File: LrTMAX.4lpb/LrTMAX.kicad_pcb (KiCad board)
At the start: 4 copper layers, 100 x 100 mm, 126 parts, among them J1 USB_C_Receptacle_USB2.0, J2 Conn_02x05_Odd_Even, Q1 2N7002, SW1 Tact_SW_8mm, SW10 EC11_SMD, SW11 EC11_SMD, SW12 EC11_SMD, SW13 EC11_SMD, SW14 EC11_SMD, SW15 EC11_SMD, SW16 EC11_SMD, SW17 EC11_SMD, SW2 Tact_SW_8mm, SW20 SW_SPST, SW3 Tact_SW_8mm, SW4 Tact_SW_8mm, SW5 Tact_SW_8mm, SW6 Tact_SW_8mm, SW7 Tact_SW_8mm, SW8 Tact_SW_8mm, U1 STM32F072C8Tx, U3 SSD1306_OLED_0.91, U4 SPX3819M5-L3-3TR

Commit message: Refine pattern.
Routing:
- net /M3: track 197.1 -> 196.4 mm
- net GND: track 46.4 -> 45.8 mm
- net /USB_DM: track 29.5 -> 28.9 mm
- net Net-(R45-Pad1): track 14.8 -> 14.2 mm
- net /ENC1B: track 80.6 -> 80.1 mm
- net /ENC4A: track 41.5 -> 41.0 mm

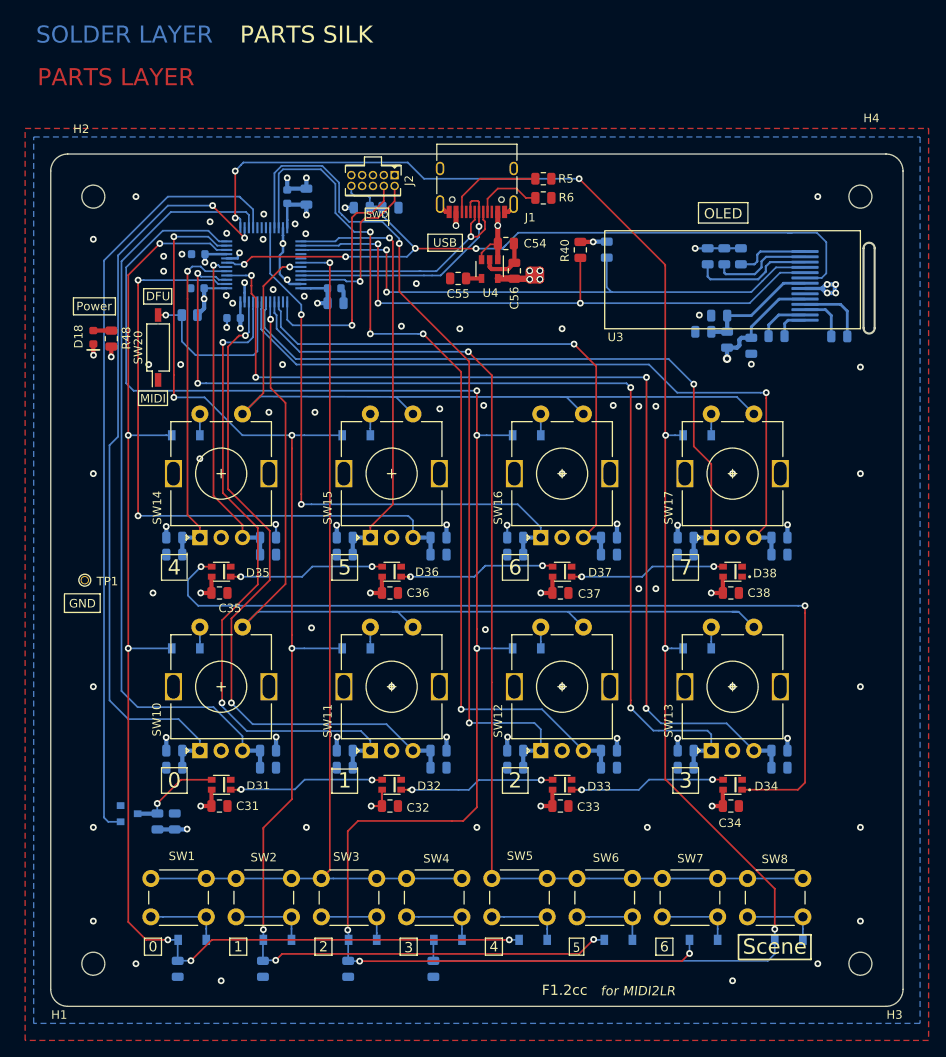
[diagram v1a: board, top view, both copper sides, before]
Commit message: Flex wire hall refined
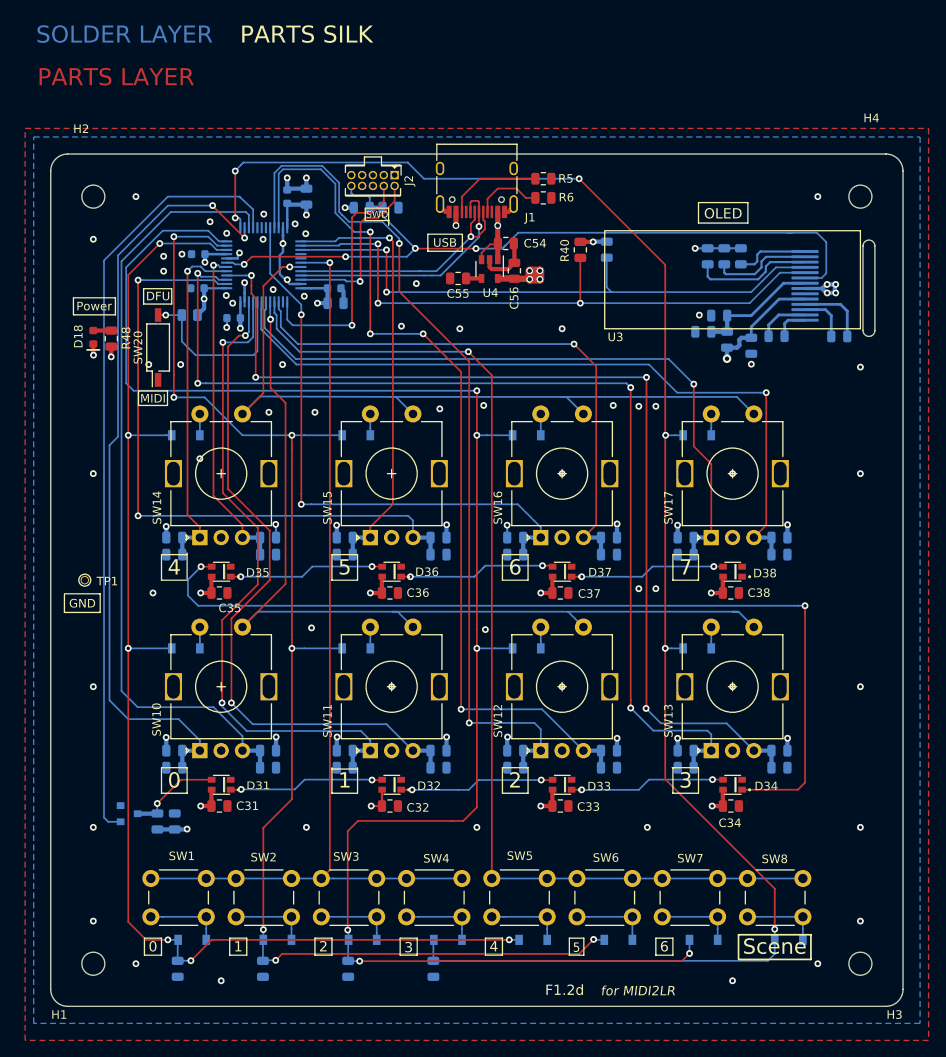
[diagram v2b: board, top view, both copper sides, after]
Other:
- outline, holes or cut-outs redrawn
- rule pad_to_mask_clearance: 0.051 -> 0
- board text added: "F1.2d"
- board text removed: "F1.2cc"
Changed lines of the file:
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@@
   )
   (setup
-    (pad_to_mask_clearance 0.051)
+    (stackup
+      (layer "F.SilkS" (type "Top Silk Screen"))
+      (layer "F.Paste" (type "Top Solder Paste"))
+      (layer "F.Mask" (type "Top Solder Mask") (color "Black") (thickness 0.01))
+      (layer "F.Cu" (type "copper") (thickness 0.035))
+      (layer "dielectric 1" (type "core") (thickness 0.48) (material "FR4") (epsilon_r 4.5) (loss_tangent 0.02))
+      (layer "In1.Cu" (type "copper") (thickness 0.035))
+      (layer "dielectric 2" (type "prepreg") (thickness 0.48) (material "FR4") (epsilon_r 4.5) (loss_tangent 0.02))
+      (layer "In2.Cu" (type "copper") (thickness 0.035))
+      (layer "dielectric 3" (type "core") (thickness 0.48) (material "FR4") (epsilon_r 4.5) (loss_tangent 0.02))
+      (layer "B.Cu" (type "copper") (thickness 0.035))
+      (layer "B.Mask" (type "Bottom Solder Mask") (color "Black") (thickness 0.01))
+      (layer "B.Paste" (type "Bottom Solder Paste"))
+      (layer "B.SilkS" (type "Bottom Silk Screen"))
+      (copper_finish "None")
+      (dielectric_constraints no)
+    )
+    (pad_to_mask_clearance 0)
     (solder_mask_min_width 0.25)
     (pcbplotparams
@@
     (fp_line (start 0 0.1) (end 0 11.5) (layer "F.SilkS") (width 0.12))
     (fp_line (start 0 11.5) (end 30 11.5) (layer "F.SilkS") (width 0.12))
-    (pad "" np_thru_hole oval locked (at 31 6.75) (size 1.6 11) (drill oval 1.2 10.4) (layers *.Mask))
+    (pad "" np_thru_hole oval locked (at 31 6.75) (size 1.6 11.5) (drill oval 1.2 11) (layers *.Mask))
     (pad "1" smd roundrect locked (at 23.5 10.5) (size 3.2 0.35) (layers "B.Cu" "B.Paste" "B.Mask") (roundrect_rratio 0.25)
       (net 66 "Net-(C49-Pad2)") (pinfunction "C2P") (pintype "passive"))
@@
     )
   )
-  (footprint "Button_Switch_SMD:SW_DIP_SPSTx01_Slide_Copal_CHS-01B_W7.62mm_P1.27mm" (layer "F.Cu")
+  (footprint "Button_Switch_SMD:SW_DIP_SPSTx01_Slide_Copal_CHS-01B_W7.62mm_P1.27mm" locked (layer "F.Cu")
     (at 112.6 122.7 90)
     (descr "SMD 1x-dip-switch SPST Copal_CHS-01B, Slide, row spacing 7.62 mm (300 mils), body size  (see http://www.nidec-copal-electronics.com/e/catalog/switch/chs.pdf), SMD")
@@
     (fp_line (start 1.5 -0.25) (end -1.5 -0.25) (layer "F.Fab") (width 0.1))
     (fp_line (start -1.5 0.05) (end -0.5 0.05) (layer "F.Fab") (width 0.1))
-    (pad "1" smd rect (at -3.81 0 90) (size 1.6 0.76) (layers "F.Cu" "F.Paste" "F.Mask")
+    (pad "1" smd rect locked (at -3.81 0 90) (size 1.6 0.76) (layers "F.Cu" "F.Paste" "F.Mask")
       (net 3 "GND") (pinfunction "A") (pintype "passive"))
-    (pad "2" smd rect (at 3.81 0 90) (size 1.6 0.76) (layers "F.Cu" "F.Paste" "F.Mask")
+    (pad "2" smd rect locked (at 3.81 0 90) (size 1.6 0.76) (layers "F.Cu" "F.Paste" "F.Mask")
       (net 78 "Net-(R7-Pad2)") (pinfunction "B") (pintype "passive"))
     (model "${KICAD6_3DMODEL_DIR}/Button_Switch_SMD.3dshapes/SW_DIP_SPSTx01_Slide_Copal_CHS-01B_W7.62mm_P1.27mm.wrl"
@@
   (gr_line (start 171 194) (end 173 194) (layer "F.SilkS") (width 0.15))
   (gr_arc (start 100 102) (mid 100.585786 100.585786) (end 102 100) (layer "Edge.Cuts") (width 0.15))
-  (gr_arc (start 196.67 120.41) (mid 196.02 121.06) (end 195.37 120.41) (layer "Edge.Cuts") (width 0.25))
-  (gr_line (start 195.37 120.41) (end 195.37 111.06) (layer "Edge.Cuts") (width 0.25))
+  (gr_line locked (start 195.3 120.7) (end 195.3 110.8) (layer "Edge.Cuts") (width 0.15))
   (gr_line (start 198 100) (end 102 100) (layer "Edge.Cuts") (width 0.15))
+  (gr_arc (start 195.3 110.8) (mid 196 110.1) (end 196.7 110.8) (layer "Edge.Cuts") (width 0.15))
   (gr_arc (start 102 200) (mid 100.585786 199.414214) (end 100 198) (layer "Edge.Cuts") (width 0.15))
-  (gr_line (start 196.67 111.06) (end 196.67 120.41) (layer "Edge.Cuts") (width 0.25))
+  (gr_line locked (start 196.7 110.8) (end 196.7 120.7) (layer "Edge.Cuts") (width 0.15))
+  (gr_arc (start 196.7 120.7) (mid 196 121.4) (end 195.3 120.7) (layer "Edge.Cuts") (width 0.15))
   (gr_line (start 102 200) (end 198 200) (layer "Edge.Cuts") (width 0.15))
   (gr_line (start 200 198) (end 200 102) (layer "Edge.Cuts") (width 0.15))
@@
   (gr_arc (start 198 100) (mid 199.414214 100.585786) (end 200 102) (layer "Edge.Cuts") (width 0.15))
   (gr_arc (start 200 198) (mid 199.414214 199.414214) (end 198 200) (layer "Edge.Cuts") (width 0.15))
-  (gr_arc (start 195.37 111.06) (mid 196.02 110.41) (end 196.67 111.06) (layer "Edge.Cuts") (width 0.25))
   (gr_text "PARTS LAYER" (at 107.65 91) (layer "F.Cu")
     (effects (font (size 2 2) (thickness 0.3)))
@@
     (effects (font (size 1.8 1.8) (thickness 0.2)))
   )
-  (gr_text "F1.2cc" (at 160.3 198.1) (layer "F.SilkS")
+  (gr_text "F1.2d" (at 160.3 198.1) (layer "F.SilkS")
     (effects (font (size 1.2 1.2) (thickness 0.22)))
   )
@@
   (segment (start 137.5 132.1968) (end 137.5 130.5) (width 0.2032) (layer "B.Cu") (net 8))
   (segment (start 154.4 114.6375) (end 156.1375 114.6375) (width 0.75) (layer "F.Cu") (net 9))
-  (segment (start 156.2 113.8) (end 156.3 113.7) (width 0.254) (layer "F.Cu") (net 9))
   (segment (start 156.2 113.7) (end 156.4 113.7) (width 0.254) (layer "F.Cu") (net 9))
   (segment (start 157.4 113.7) (end 157.2 113.7) (width 0.254) (layer "F.Cu") (net 9))
@@
   (segment (start 152.45 114.6) (end 154.3625 114.6) (width 0.75) (layer "F.Cu") (net 9))
   (segment (start 156.1375 114.6375) (end 156.2 114.7) (width 0.254) (layer "F.Cu") (net 9))
-  (segment (start 156.3 114.6) (end 156.2 114.7) (width 0.254) (layer "F.Cu") (net 9))
   (segment (start 157.4 113.7) (end 157.4 114.7) (width 1) (layer "F.Cu") (net 9))
   (segment (start 156.2 114.7) (end 157.4 114.7) (width 1) (layer "F.Cu") (net 9))
@@
   (segment (start 186.4375 143.5125) (end 186.45 143.5) (width 0.254) (layer "B.Cu") (net 9))
   (segment (start 166.4375 143.4125) (end 166.45 143.4) (width 0.254) (layer "B.Cu") (net 9))
-  (segment (start 150 133) (end 150 133) (width 0.2032) (layer "F.Cu") (net 10))
   (segment (start 150 176.65) (end 150 158) (width 0.2032) (layer "F.Cu") (net 10))
   (segment (start 150 155.7) (end 150 133) (width 0.2032) (layer "F.Cu") (net 10))
@@
   (via (at 124.95 191) (size 0.8) (drill 0.4) (layers "F.Cu" "B.Cu") (net 11))
   (via (at 128.3 133) (size 0.8) (drill 0.4) (layers "F.Cu" "B.Cu") (net 11))
-  (segment (start 114.45 109.7) (end 114.45 109.7) (width 0.2032) (layer "B.Cu") (net 11))
   (segment (start 129.75 158) (end 134.2 158) (width 0.2032) (layer "B.Cu") (net 11))
   (segment (start 120.65 110.75) (end 119.535909 110.75) (width 0.2032) (layer "B.Cu") (net 11))
@@
   (segment (start 139.4 116.2) (end 165.8 116.2) (width 0.2032) (layer "B.Cu") (net 12))
   (segment (start 182.2 116.2) (end 183.5 114.9) (width 0.2032) (layer "B.Cu") (net 12))
-  (segment (start 138.400001 110.548402) (end 138.399999 110.5484) (width 0.2032) (layer "F.Cu") (net 13))
   (segment (start 162.14 112.185) (end 162.14 117.5) (width 0.2032) (layer "F.Cu") (net 13))
   (segment (start 138.399999 110.5484) (end 138.399999 117.5) (width 0.2032) (layer "F.Cu") (net 13))
@@
   (segment (start 144.9 194.6625) (end 144.9 192) (width 0.2032) (layer "B.Cu") (net 15))
   (segment (start 143.8 102.9) (end 156.1 102.9) (width 0.2032) (layer "B.Cu") (net 15))
-  (segment (start 112.8 110.5) (end 112.8 110.5) (width 0.2032) (layer "F.Cu") (net 16))
   (segment (start 109.1 158) (end 109.1 133) (width 0.2032) (layer "F.Cu") (net 16))
   (segment (start 118.9 192.2) (end 116.45 194.65) (width 0.2032) (layer "F.Cu") (net 16))
@@
   (segment (start 126.25 102.229775) (end 126.25 108.65) (width 0.2032) (layer "B.Cu") (net 48))
   (segment (start 148.15 165.15) (end 148.15 125.55) (width 0.2032) (layer "F.Cu") (net 49))
-  (segment (start 137.5 109.249998) (end 137.5 109.145199) (width 0.2032) (layer "F.Cu") (net 49))
   (segment (start 148.15 125.55) (end 143.7 121.1) (width 0.2032) (layer "F.Cu") (net 49))
-  (segment (start 137.500001 109.249999) (end 137.5 109.249998) (width 0.2032) (layer "F.Cu") (net 49))
   (segment (start 137.5 121.1) (end 137.5 120.534315) (width 0.2032) (layer "F.Cu") (net 49))
   (segment (start 137.5 120.534315) (end 137.5 109.145199) (width 0.2032) (layer "F.Cu") (net 49))
@@
     (polygon
       (pts
-        (xy 195.584867 109.806695)
-        (xy 194.984867 110.206695)
+        (xy 195.6 109.7)
+        (xy 194.984867 110.1)
         (xy 194.684867 110.806695)
-        (xy 194.784867 120.806695)
-        (xy 195.084867 121.406695)
-        (xy 195.584867 121.806695)
-        (xy 196.484867 121.806695)
-        (xy 196.884867 121.506695)
-        (xy 197.184867 121.106695)
-        (xy 197.264867 120.756695)
-        (xy 197.284867 110.606695)
-        (xy 196.984867 110.106695)
-        (xy 196.484867 109.806695)
+        (xy 194.7 120.7)
+        (xy 195 121.4)
+        (xy 195.584867 121.9)
+        (xy 196.5 121.9)
+        (xy 196.9 121.6)
+        (xy 197.1 121.3)
+        (xy 197.264867 120.8)
+        (xy 197.3 110.8)
+        (xy 197 110.1)
+        (xy 196.484867 109.7)
       )
     )
